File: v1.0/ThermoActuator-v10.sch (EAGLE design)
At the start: 75 parts, among them IC1 ULN2003AD, IC2 LM358D, IC3 LM358D, IC4 LM358D, IC5 LM358D

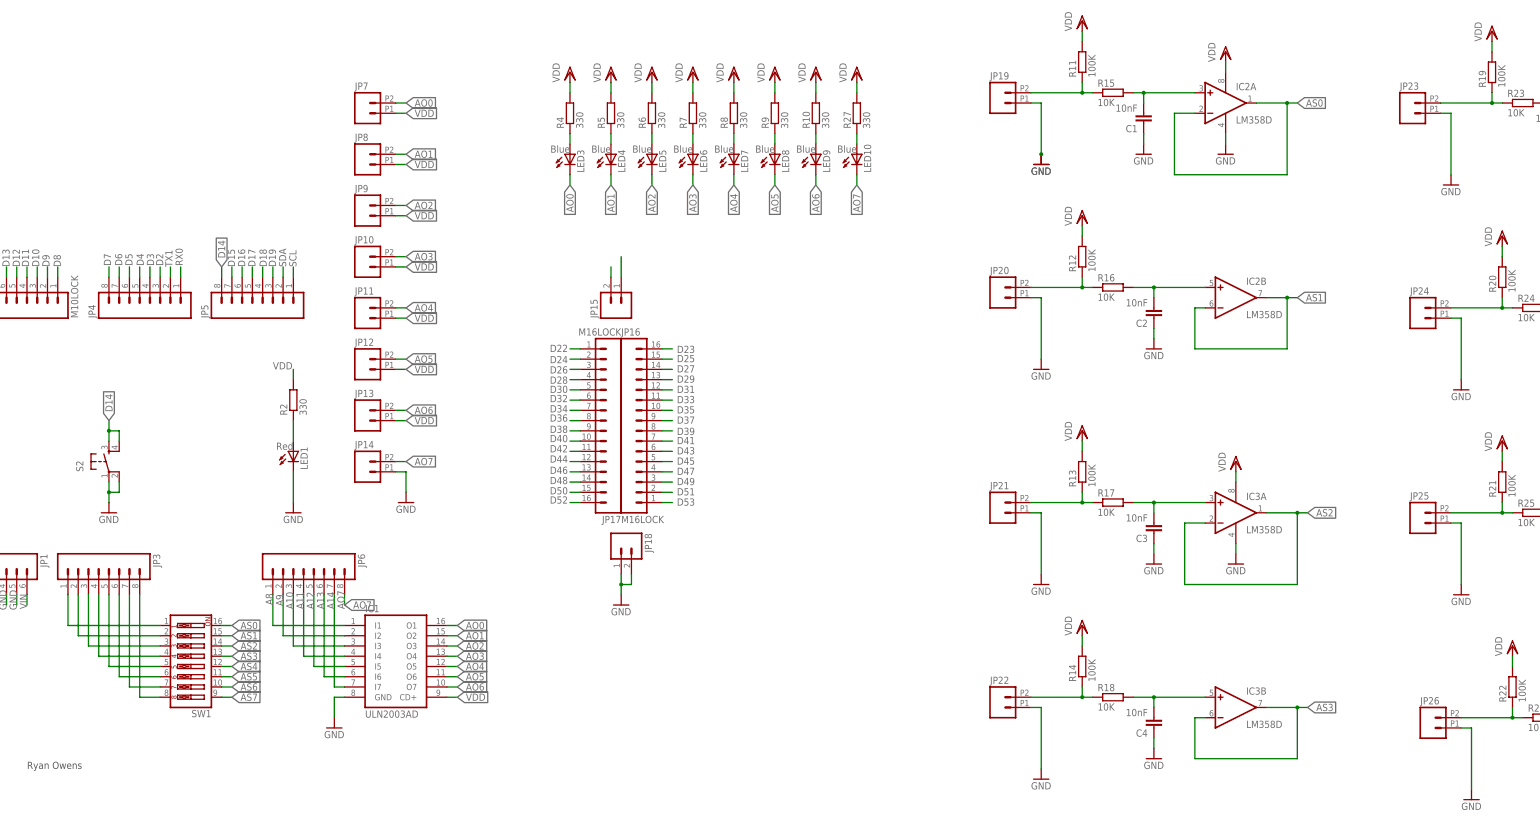
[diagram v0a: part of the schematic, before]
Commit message: button removed. Ready for manufacturing
the button is removed. It will sit on the top layer (RTC & SD shield)

Screw terminals replace with pitch 5.

Thermistor terminals moved to upper lane

the board is ready for production, a request for quotation is sent
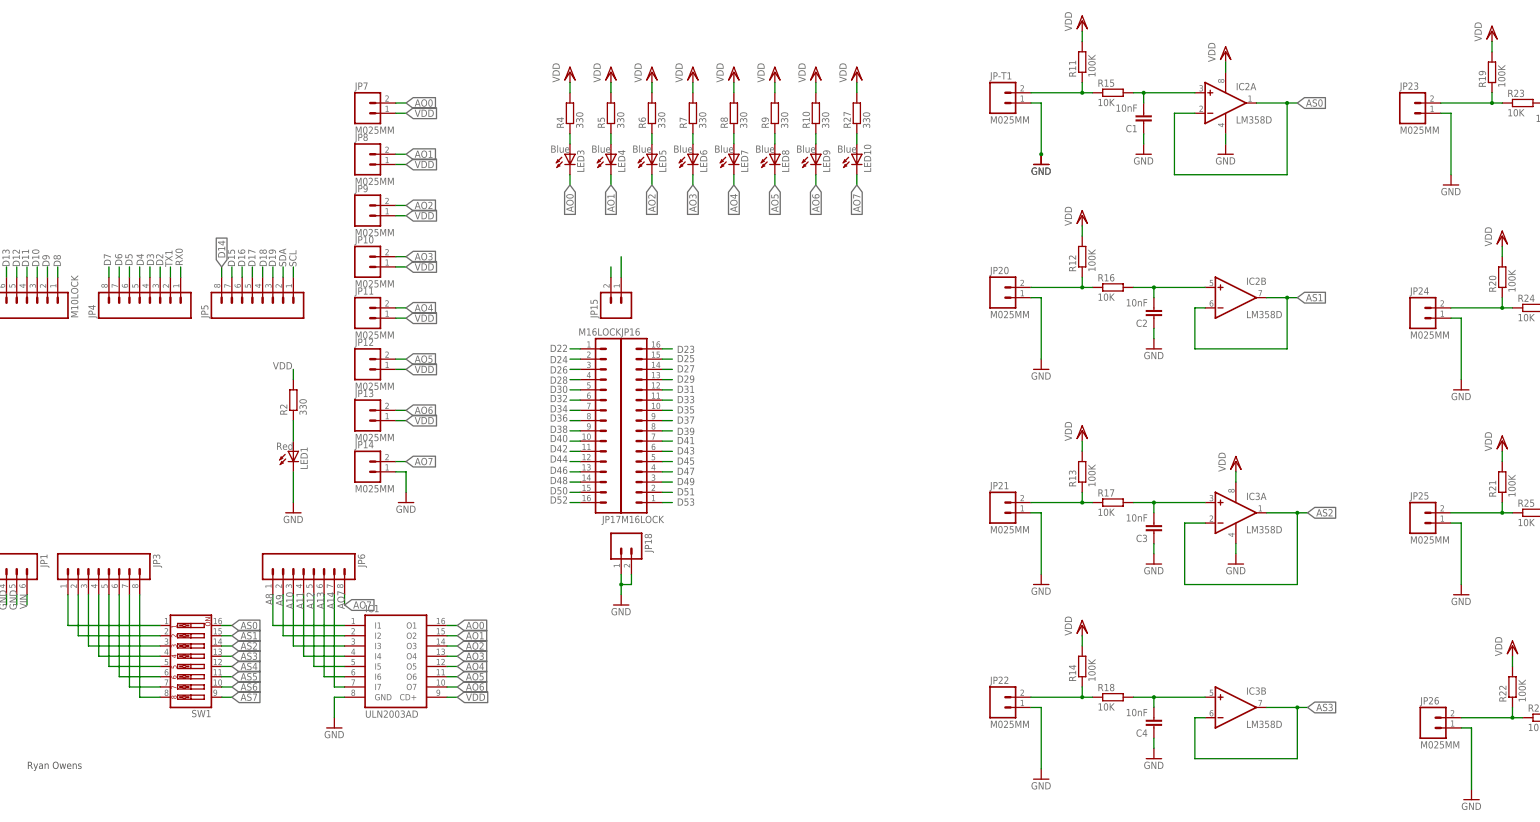
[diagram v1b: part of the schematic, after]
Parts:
- removed JP19: M022.54MM_SCREWTERM, SparkFun-Connectors:M022.54MM_SCREWTERM
- removed S2: (no value), SparkFun:TAC_SWITCHPTH
- added JP-T1: M025MM, SparkFun-Connectors:M025MM
- JP10, JP11, JP12, JP13, JP14, JP20, JP21, JP22, JP23, JP24, JP25, JP26, JP7, JP8, JP9: value M022.54MM_SCREWTERM -> M025MM; device SparkFun-Connectors:M022.54MM_SCREWTERM -> SparkFun-Connectors:M025MM
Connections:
- net D14: no longer S2.3, S2.4
- net GND: now also JP-T1.1; no longer JP19.1, S2.1, S2.2
- net N$1: now also JP-T1.2; no longer JP19.2
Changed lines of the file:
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@@
 <part name="R10" library="rcl" deviceset="R-EU_" device="R0805" value="330"/>
 <part name="VDD7" library="supply1" deviceset="VDD" device=""/>
-<part name="JP19" library="SparkFun-Connectors" deviceset="M02" device="2.54MM_SCREWTERM" value=""/>
-<part name="JP20" library="SparkFun-Connectors" deviceset="M02" device="2.54MM_SCREWTERM" value=""/>
-<part name="JP7" library="SparkFun-Connectors" deviceset="M02" device="2.54MM_SCREWTERM" value=""/>
-<part name="JP8" library="SparkFun-Connectors" deviceset="M02" device="2.54MM_SCREWTERM" value=""/>
-<part name="JP9" library="SparkFun-Connectors" deviceset="M02" device="2.54MM_SCREWTERM" value=""/>
-<part name="JP10" library="SparkFun-Connectors" deviceset="M02" device="2.54MM_SCREWTERM" value=""/>
-<part name="JP11" library="SparkFun-Connectors" deviceset="M02" device="2.54MM_SCREWTERM" value=""/>
-<part name="JP12" library="SparkFun-Connectors" deviceset="M02" device="2.54MM_SCREWTERM" value=""/>
-<part name="JP13" library="SparkFun-Connectors" deviceset="M02" device="2.54MM_SCREWTERM" value=""/>
-<part name="JP14" library="SparkFun-Connectors" deviceset="M02" device="2.54MM_SCREWTERM" value=""/>
+<part name="JP-T1" library="SparkFun-Connectors" deviceset="M02" device="5MM" value="M025MM"/>
+<part name="JP20" library="SparkFun-Connectors" deviceset="M02" device="5MM" value="M025MM"/>
+<part name="JP7" library="SparkFun-Connectors" deviceset="M02" device="5MM" value="M025MM"/>
+<part name="JP8" library="SparkFun-Connectors" deviceset="M02" device="5MM" value="M025MM"/>
+<part name="JP9" library="SparkFun-Connectors" deviceset="M02" device="5MM" value="M025MM"/>
+<part name="JP10" library="SparkFun-Connectors" deviceset="M02" device="5MM" value="M025MM"/>
+<part name="JP11" library="SparkFun-Connectors" deviceset="M02" device="5MM" value="M025MM"/>
+<part name="JP12" library="SparkFun-Connectors" deviceset="M02" device="5MM" value="M025MM"/>
+<part name="JP13" library="SparkFun-Connectors" deviceset="M02" device="5MM" value="M025MM"/>
+<part name="JP14" library="SparkFun-Connectors" deviceset="M02" device="5MM" value="M025MM"/>
 <part name="IC3" library="linear" deviceset="LM358" device="D"/>
 <part name="GND8" library="supply1" deviceset="GND" device=""/>
@@
 <part name="C3" library="rcl" deviceset="C-EU" device="C1206" value="10nF"/>
 <part name="GND12" library="supply1" deviceset="GND" device=""/>
-<part name="JP21" library="SparkFun-Connectors" deviceset="M02" device="2.54MM_SCREWTERM" value=""/>
+<part name="JP21" library="SparkFun-Connectors" deviceset="M02" device="5MM" value="M025MM"/>
 <part name="VDD13" library="supply1" deviceset="VDD" device=""/>
 <part name="GND15" library="supply1" deviceset="GND" device=""/>
@@
 <part name="C4" library="rcl" deviceset="C-EU" device="C1206" value="10nF"/>
 <part name="GND13" library="supply1" deviceset="GND" device=""/>
-<part name="JP22" library="SparkFun-Connectors" deviceset="M02" device="2.54MM_SCREWTERM" value=""/>
+<part name="JP22" library="SparkFun-Connectors" deviceset="M02" device="5MM" value="M025MM"/>
 <part name="IC4" library="linear" deviceset="LM358" device="D"/>
 <part name="GND16" library="supply1" deviceset="GND" device=""/>
@@
 <part name="C5" library="rcl" deviceset="C-EU" device="C1206" value="10nF"/>
 <part name="GND20" library="supply1" deviceset="GND" device=""/>
-<part name="JP23" library="SparkFun-Connectors" deviceset="M02" device="2.54MM_SCREWTERM" value=""/>
+<part name="JP23" library="SparkFun-Connectors" deviceset="M02" device="5MM" value="M025MM"/>
 <part name="VDD18" library="supply1" deviceset="VDD" device=""/>
 <part name="GND24" library="supply1" deviceset="GND" device=""/>
@@
 <part name="C6" library="rcl" deviceset="C-EU" device="C1206" value="10nF"/>
 <part name="GND21" library="supply1" deviceset="GND" device=""/>
-<part name="JP24" library="SparkFun-Connectors" deviceset="M02" device="2.54MM_SCREWTERM" value=""/>
+<part name="JP24" library="SparkFun-Connectors" deviceset="M02" device="5MM" value="M025MM"/>
 <part name="IC5" library="linear" deviceset="LM358" device="D"/>
 <part name="GND18" library="supply1" deviceset="GND" device=""/>
@@
 <part name="C7" library="rcl" deviceset="C-EU" device="C1206" value="10nF"/>
 <part name="GND22" library="supply1" deviceset="GND" device=""/>
-<part name="JP25" library="SparkFun-Connectors" deviceset="M02" device="2.54MM_SCREWTERM" value=""/>
+<part name="JP25" library="SparkFun-Connectors" deviceset="M02" device="5MM" value="M025MM"/>
 <part name="VDD19" library="supply1" deviceset="VDD" device=""/>
 <part name="GND25" library="supply1" deviceset="GND" device=""/>
@@
 <part name="C8" library="rcl" deviceset="C-EU" device="C1206" value="10nF"/>
 <part name="GND23" library="supply1" deviceset="GND" device=""/>
-<part name="JP26" library="SparkFun-Connectors" deviceset="M02" device="2.54MM_SCREWTERM" value=""/>
-<part name="S2" library="SparkFun" deviceset="TAC_SWITCH" device="PTH"/>
-<part name="GND26" library="SparkFun" deviceset="GND" device=""/>
+<part name="JP26" library="SparkFun-Connectors" deviceset="M02" device="5MM" value="M025MM"/>
 <part name="LED10" library="led" deviceset="LED" device="CHIP-LED0805" value="Blue"/>
 <part name="R27" library="rcl" deviceset="R-EU_" device="R0805" value="330"/>
@@
 <instance part="R10" gate="G$1" x="226.06" y="172.72" rot="R90"/>
 <instance part="VDD7" gate="G$1" x="226.06" y="182.88"/>
-<instance part="JP19" gate="G$1" x="271.78" y="175.26"/>
+<instance part="JP-T1" gate="G$1" x="271.78" y="175.26"/>
 <instance part="JP20" gate="G$1" x="271.78" y="127"/>
 <instance part="JP7" gate="G$1" x="114.3" y="172.72"/>
@@
 <instance part="GND23" gate="1" x="416.56" y="7.62"/>
 <instance part="JP26" gate="G$1" x="378.46" y="20.32"/>
-<instance part="S2" gate="S" x="50.8" y="86.36" rot="R90"/>
-<instance part="GND26" gate="1" x="50.8" y="73.66"/>
 <instance part="LED10" gate="G$1" x="236.22" y="162.56" smashed="yes">
 <attribute name="NAME" x="239.776" y="157.988" size="1.778" layer="95" rot="R90"/>
@@
 <pinref part="GND5" gate="1" pin="GND"/>
 <pinref part="GND6" gate="1" pin="GND"/>
-<pinref part="JP19" gate="G$1" pin="1"/>
+<pinref part="JP-T1" gate="G$1" pin="1"/>
 <wire x1="279.4" y1="175.26" x2="281.94" y2="175.26" width="0.1524" layer="91"/>
 <wire x1="281.94" y1="175.26" x2="281.94" y2="162.56" width="0.1524" layer="91"/>
@@
 <pinref part="C8" gate="G$1" pin="1"/>
 <wire x1="416.56" y1="10.16" x2="416.56" y2="12.7" width="0.1524" layer="91"/>
-</segment>
-<segment>
-<pinref part="S2" gate="S" pin="1"/>
-<pinref part="GND26" gate="1" pin="GND"/>
-<wire x1="50.8" y1="81.28" x2="50.8" y2="78.74" width="0.1524" layer="91"/>
-<pinref part="S2" gate="S" pin="2"/>
-<wire x1="50.8" y1="78.74" x2="50.8" y2="76.2" width="0.1524" layer="91"/>
-<wire x1="53.34" y1="81.28" x2="53.34" y2="78.74" width="0.1524" layer="91"/>
-<wire x1="53.34" y1="78.74" x2="50.8" y2="78.74" width="0.1524" layer="91"/>
-<junction x="50.8" y="78.74"/>
 </segment>
 </net>
@@
 <wire x1="78.74" y1="132.08" x2="78.74" y2="134.62" width="0.1524" layer="91"/>
 <label x="78.74" y="134.62" size="1.778" layer="95" rot="R90" xref="yes"/>
-</segment>
-<segment>
-<pinref part="S2" gate="S" pin="3"/>
-<wire x1="50.8" y1="91.44" x2="50.8" y2="93.98" width="0.1524" layer="91"/>
-<pinref part="S2" gate="S" pin="4"/>
-<wire x1="53.34" y1="91.44" x2="53.34" y2="93.98" width="0.1524" layer="91"/>
-<wire x1="53.34" y1="93.98" x2="50.8" y2="93.98" width="0.1524" layer="91"/>
-<wire x1="50.8" y1="93.98" x2="50.8" y2="96.52" width="0.1524" layer="91"/>
-<junction x="50.8" y="93.98"/>
-<label x="50.8" y="96.52" size="1.778" layer="95" rot="R90" xref="yes"/>
 </segment>
 </net>
@@
 <wire x1="292.1" y1="180.34" x2="292.1" y2="177.8" width="0.1524" layer="91"/>
 <junction x="292.1" y="177.8"/>
-<pinref part="JP19" gate="G$1" pin="2"/>
-</segment>
-</net>
+<pinref part="JP-T1" gate="G$1" pin="2"/>
+</segment>
+</net>
